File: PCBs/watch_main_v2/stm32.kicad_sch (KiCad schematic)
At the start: 20 parts, among them U801 STM32U5A9NJH6Q, Y801 16MHz, Y802 32.768kHz

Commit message: Schematic v2 complete
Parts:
- added R807, R808, R809, R810: 4k7, Resistor_SMD:R_0402_1005Metric, symbol Device:R_Small
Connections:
- net SWCLK is gone; now on net SWD.SWCLK: TP806.1
- net SWDIO is gone; now on net SWD.SWDIO: TP805.1
- net +1V8: now also R801.1, R802.1, R809.1, R810.1
- net +3V3: now also R807.1, R808.1; no longer R801.1, R802.1
- net ADF1_CCK0: now also U801.P9 (PE9)
- net ADF1_SDI0: now also U801.P10 (PE10)
- net CRS_SYNC: now also U801.D12 (PA10)
- net FLASH_CS2: now also U801.N4 (PA0)
- net I2C1.SCL: now also U801.D7 (PG14), R807.2; no longer R801.2
- net I2C1.SDA: now also U801.B6 (PG13), R808.2; no longer R802.2
- net I2C3.SCL: now also U801.P2 (PC0)
- net I2C3.SDA: now also U801.M1 (PC1)
- net I2C4.SCL: now also U801.M13 (PD12)
- net I2C4.SDA: now also U801.N14 (PD13)
- net LPUART1.RX: now also U801.E13 (PG8)
- net LPUART1.TX: now also U801.D13 (PG7)
- net LPUART1_CTS: now also U801.E14 (PG5)
- net LPUART1_RTS: now also U801.M6 (PB1)
- net OSPI1.CLKN: now also U801.M11 (PB12)
- net OSPI1.CLKP: now also U801.N12 (PB10)
- net OSPI1.CS: now also U801.P11 (PE11)
- net OSPI1.DQS: now also U801.D14 (PG6)
- net OSPI1.IO0: now also U801.J14 (PI3)
- net OSPI1.IO1: now also U801.J13 (PI2)
- net OSPI1.IO2: now also U801.J12 (PI1)
- net OSPI1.IO3: now also U801.D10 (PH8)
- net OSPI1.IO4: now also U801.M14 (PH9)
- net OSPI1.IO5: now also U801.L13 (PH10)
- net OSPI1.IO6: now also U801.L14 (PH11)
- net OSPI1.IO7: now also U801.M15 (PH12)
- net SDMMC1.CK: now also U801.C10 (PC12)
- net SDMMC1.CKIN: now also U801.C6 (PB8)
- net SDMMC1.CMD: now also U801.B9 (PD2)
- net SDMMC1.D0: now also U801.A14 (PC8)
- net SDMMC1.D1: now also U801.C14 (PC9)
- net SDMMC1.D2: now also U801.A10 (PC10)
- net SDMMC1.D3: now also U801.B10 (PC11)
- net SWO: now also U801.E7 (PB3)
- net USART6.RX: now also U801.P1 (PC2); no longer TP803.1
- net USART6.TX: now also U801.N3 (PC3); no longer TP802.1
- net SWD.SWCLK: now reaches U801.A12 (PA14)
- net USART1.RX: now reaches U801.A3 (PB7)
- net USART1.TX: now reaches U801.A4 (PB6)
- net USB.DP: now reaches U801.B13 (PA12)
- net USB.DN: now reaches U801.B14 (PA11)
- net SWD.SWDIO: now reaches U801.C13 (PA13)
- net GPIO2: now reaches U801.C9 (PD1)
- net GPIO1: now reaches U801.D9 (PD0)
- net I2C2.SCL: now reaches U801.M12 (PB13)
- net I2C2.SCL: now also R801.2
- net SPI1.CS: now reaches U801.N6 (PB0)
- net I2C2.SDA: now reaches U801.P13 (PB14)
- net I2C2.SDA: now also R802.2
- net SPI1.MISO: now reaches U801.P5 (PA6)
- net SPI1.SCK: now reaches U801.R4 (PA5)
- net SPI1.MOSI: now reaches U801.R5 (PA7)
- net I2C6.SCL: now reaches U801.F1 (PJ10)
- net I2C6.SCL: now also R809.2
- net I2C6.SDA: now reaches U801.H3 (PF0)
- net I2C6.SDA: now also R810.2
- net NRST renamed SWD.RST
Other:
- removed sheet STM32 Power
- moved on the sheet: C801, C802, C803, C804, R801, R802, R803, R804, R805, R806, TP804, TP805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

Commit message: 252 Unrouted traces
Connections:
- net GNSS_RST: now also U801.D1 (PJ3)
- net GNSS_WAKEUP: now also U801.E2 (PJ6)
- net TP_INT: now also U801.F2 (PJ8)
- net TP_RST: now also U801.E1 (PJ7)
- no-connect marks 4 -> 11
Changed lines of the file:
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@@
   (junction (at 243.84 236.22) (diameter 0) (color 0 0 0 0)
   )
+  (no_connect (at 195.58 157.48))
+  (no_connect (at 144.78 119.38))
   (no_connect (at 287.02 60.96))
+  (no_connect (at 144.78 109.22))
   (no_connect (at 287.02 63.5))
   (no_connect (at 287.02 81.28))
+  (no_connect (at 195.58 170.18))
+  (no_connect (at 195.58 60.96))
+  (no_connect (at 337.82 106.68))
   (no_connect (at 287.02 78.74))
+  (no_connect (at 195.58 167.64))
   (bus_entry (at 50.8 205.74) (size -2.54 2.54)
     (stroke (width 0) (type default))
@@
     (stroke (width 0) (type default))
   )
+  (wire (pts (xy 116.84 154.94) (xy 144.78 154.94))
+    (stroke (width 0) (type default))
+  )
   (wire (pts (xy 35.56 182.88) (xy 48.26 182.88))
     (stroke (width 0) (type default))
@@
     (stroke (width 0) (type default))
   )
-  (wire (pts (xy -15.24 83.82) (xy -43.18 83.82))
+  (wire (pts (xy 116.84 162.56) (xy 144.78 162.56))
     (stroke (width 0) (type default))
   )
@@
     (stroke (width 0) (type default))
   )
-  (wire (pts (xy -88.9 203.2) (xy -68.58 203.2))
-    (stroke (width 0) (type default))
-  )
   (wire (pts (xy 223.52 86.36) (xy 195.58 86.36))
     (stroke (width 0) (type default))
@@
     (stroke (width 0) (type default))
   )
+  (wire (pts (xy 116.84 165.1) (xy 144.78 165.1))
+    (stroke (width 0) (type default))
+  )
   (bus (pts (xy 50.8 50.8) (xy 71.12 50.8))
     (stroke (width 0) (type default))
@@
     (stroke (width 0) (type default))
   )
-  (wire (pts (xy -88.9 210.82) (xy -68.58 210.82))
-    (stroke (width 0) (type default))
-  )
   (wire (pts (xy 35.56 134.62) (xy 48.26 134.62))
     (stroke (width 0) (type default))
@@
     (stroke (width 0) (type default))
   )
+  (wire (pts (xy 116.84 167.64) (xy 144.78 167.64))
+    (stroke (width 0) (type default))
+  )
   (wire (pts (xy 337.82 160.02) (xy 363.22 160.02))
     (stroke (width 0) (type default))
@@
   )
   (wire (pts (xy 261.62 104.14) (xy 287.02 104.14))
-    (stroke (width 0) (type default))
-  )
-  (wire (pts (xy -99.06 96.52) (xy -71.12 96.52))
     (stroke (width 0) (type default))
   )
@@
     (effects (font (size 1.27 1.27)) (justify left bottom))
   )
+  (label "GNSS_RST" (at 119.38 154.94 0) (fields_autoplaced)
+    (effects (font (size 1.27 1.27)) (justify left bottom))
+  )
   (label "FLASH_INT" (at -15.24 195.58 180) (fields_autoplaced)
     (effects (font (size 1.27 1.27)) (justify right bottom))
@@
     (effects (font (size 1.27 1.27)) (justify right bottom))
   )
-  (label "GNSS_RST" (at -73.66 96.52 180) (fields_autoplaced)
-    (effects (font (size 1.27 1.27)) (justify right bottom))
-  )
   (label "DEBUG_LED" (at -15.24 157.48 180) (fields_autoplaced)
     (effects (font (size 1.27 1.27)) (justify right bottom))
@@
     (effects (font (size 1.27 1.27)) (justify left bottom))
   )
-  (label "GNSS_WAKEUP" (at -17.78 83.82 180) (fields_autoplaced)
-    (effects (font (size 1.27 1.27)) (justify right bottom))
+  (label "GNSS_WAKEUP" (at 119.38 162.56 0) (fields_autoplaced)
+    (effects (font (size 1.27 1.27)) (justify left bottom))
   )
   (label "I2C1.SDA" (at 35.56 144.78 0) (fields_autoplaced)
@@
     (effects (font (size 1.27 1.27)) (justify left bottom))
   )
-  (label "TP_INT" (at -86.36 210.82 0) (fields_autoplaced)
+  (label "TP_INT" (at 119.38 167.64 0) (fields_autoplaced)
     (effects (font (size 1.27 1.27)) (justify left bottom))
   )
@@
     (effects (font (size 1.27 1.27)) (justify left bottom))
   )
+  (label "TP_RST" (at 119.38 165.1 0) (fields_autoplaced)
+    (effects (font (size 1.27 1.27)) (justify left bottom))
+  )
   (label "IMU_INT1" (at -15.24 165.1 180) (fields_autoplaced)
     (effects (font (size 1.27 1.27)) (justify right bottom))
@@
   )
   (label "I2C2.SCL" (at 35.56 152.4 0) (fields_autoplaced)
-    (effects (font (size 1.27 1.27)) (justify left bottom))
-  )
-  (label "TP_RST" (at -86.36 203.2 0) (fields_autoplaced)
     (effects (font (size 1.27 1.27)) (justify left bottom))
   )
@@
     )
   )
-  (hierarchical_label "TP_INT" (shape input) (at -88.9 210.82 180) (fields_autoplaced)
+  (hierarchical_label "TP_INT" (shape input) (at 116.84 167.64 180) (fields_autoplaced)
     (effects (font (size 1.27 1.27)) (justify right))
   )
@@
     (effects (font (size 1.27 1.27)) (justify left))
   )
-  (hierarchical_label "GNSS_WAKEUP" (shape output) (at -15.24 83.82 0) (fields_autoplaced)
-    (effects (font (size 1.27 1.27)) (justify left))
+  (hierarchical_label "GNSS_WAKEUP" (shape output) (at 116.84 162.56 180) (fields_autoplaced)
+    (effects (font (size 1.27 1.27)) (justify right))
   )
   (hierarchical_label "CRS_SYNC" (shape input) (at 365.76 111.76 0) (fields_autoplaced)
     (effects (font (size 1.27 1.27)) (justify left))
-  )
-  (hierarchical_label "TP_RST" (shape output) (at -88.9 203.2 180) (fields_autoplaced)
-    (effects (font (size 1.27 1.27)) (justify right))
   )
   (hierarchical_label "BT_INT1" (shape bidirectional) (at -73.66 167.64 0) (fields_autoplaced)
@@
     )
   )
+  (hierarchical_label "TP_RST" (shape output) (at 116.84 165.1 180) (fields_autoplaced)
+    (effects (font (size 1.27 1.27)) (justify right))
+  )
   (hierarchical_label "GPIO2" (shape bidirectional) (at 259.08 132.08 180) (fields_autoplaced)
     (effects (font (size 1.27 1.27)) (justify right))
@@
     (effects (font (size 1.27 1.27)) (justify right))
   )
+  (hierarchical_label "GNSS_RST" (shape output) (at 116.84 154.94 180) (fields_autoplaced)
+    (effects (font (size 1.27 1.27)) (justify right))
+  )
   (hierarchical_label "FLASH_RSTO" (shape input) (at -12.7 193.04 0) (fields_autoplaced)
     (effects (font (size 1.27 1.27)) (justify left))
@@
     (effects (font (size 1.27 1.27)) (justify left))
   )
-  (hierarchical_label "GNSS_RST" (shape output) (at -71.12 96.52 0) (fields_autoplaced)
-    (effects (font (size 1.27 1.27)) (justify left))
-  )

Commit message: 262 Unrouted traces, fixed clearance issues
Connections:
- no-connect marks 11 -> 15
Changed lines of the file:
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@@
     (rev "2")
   )
+  (bus_alias "QSPI" (members "SCK" "IO0" "IO1" "IO2" "IO3" "CS"))
+  (bus_alias "I2C" (members "SCL" "SDA"))
+  (bus_alias "DSI-1" (members "CKN" "CKP" "D0N" "D0P"))
   (bus_alias "SDIO" (members "CK" "CKIN" "D0" "D1" "D2" "D3" "CMD"))
+  (bus_alias "USB" (members "DP" "DN"))
   (bus_alias "UART" (members "TX" "RX"))
-  (bus_alias "QSPI" (members "SCK" "IO0" "IO1" "IO2" "IO3" "CS"))
+  (bus_alias "SPI" (members "SCK" "MISO" "MOSI" "CS"))
   (bus_alias "DSI-2" (members "CKN" "CKP" "D0N" "D0P" "D1N" "D1P"))
-  (bus_alias "USB" (members "DP" "DN"))
-  (bus_alias "I2C" (members "SCL" "SDA"))
-  (bus_alias "SPI" (members "SCK" "MISO" "MOSI" "CS"))
-  (bus_alias "DSI-1" (members "CKN" "CKP" "D0N" "D0P"))
   (junction (at 144.78 251.46) (diameter 0) (color 0 0 0 0)
   )
@@
   (no_connect (at 287.02 60.96))
   (no_connect (at 144.78 109.22))
+  (no_connect (at 195.58 66.04))
+  (no_connect (at 195.58 162.56))
   (no_connect (at 287.02 63.5))
   (no_connect (at 287.02 81.28))
@@
   (no_connect (at 195.58 60.96))
   (no_connect (at 337.82 106.68))
+  (no_connect (at 337.82 162.56))
+  (no_connect (at 287.02 147.32))
   (no_connect (at 287.02 78.74))
   (no_connect (at 195.58 167.64))

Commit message: 190 Unrouted traces
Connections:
- net ALS_INT: now also U801.M2 (PF6)
- net BTN: now also U801.M8 (PE8)
- net HR_INT: now also U801.N15 (PD14)
- net IMU_INT1: now also U801.R7 (PB2)
- net IMU_INT2: now also U801.R8 (PF14)
- net LRA_EN: now also U801.P15 (PD9)
- net MAG_INT: now also U801.R6 (PC4)
- net PWR_ENCHG: now also U801.R14 (PB15)
- net PWR_INT: now also U801.P14 (PD10)
- net TOUCH_INT: now also U801.N9 (PE7)
- net TOUCH_RST: now also U801.N11 (PE12)
- no-connect marks 15 -> 28

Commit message: Main board v2 complete
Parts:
- removed TP801, TP802, TP803: 1.5mm, TestPoint:TestPoint_Pad_D1.5mm, symbol Connector:TestPoint_Small
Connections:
- net AVDDEN: now also U801.A7 (PG9)
- net BT_INT1: now also U801.B15 (PC7)
- net BT_INT2: now also U801.C15 (PC6)
- net DISPLAY_RST: now also U801.L3 (PF7)
- net FLASH_INT: now also U801.F15 (PI13)
- net FLASH_RST: now also U801.F14 (PI14)
- net FLASH_RSTO: now also U801.G15 (PI10)
- net SD_CD: now also U801.A9 (PD3)
- net SWIRE: now also U801.A6 (PG12), U801.B7 (PG10)
- net SD_EN: now reaches U801.A8 (PD4)
- no-connect marks 28 -> 76

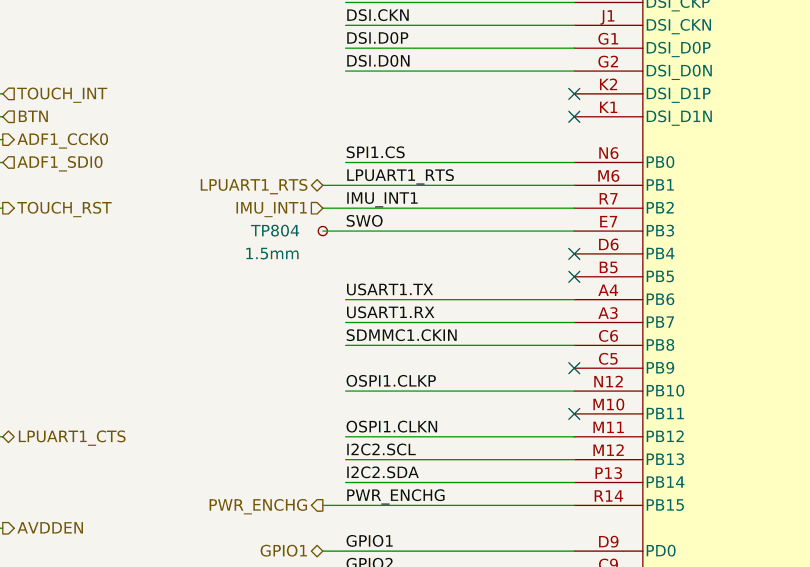
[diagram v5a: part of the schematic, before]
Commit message: Added EEPROM
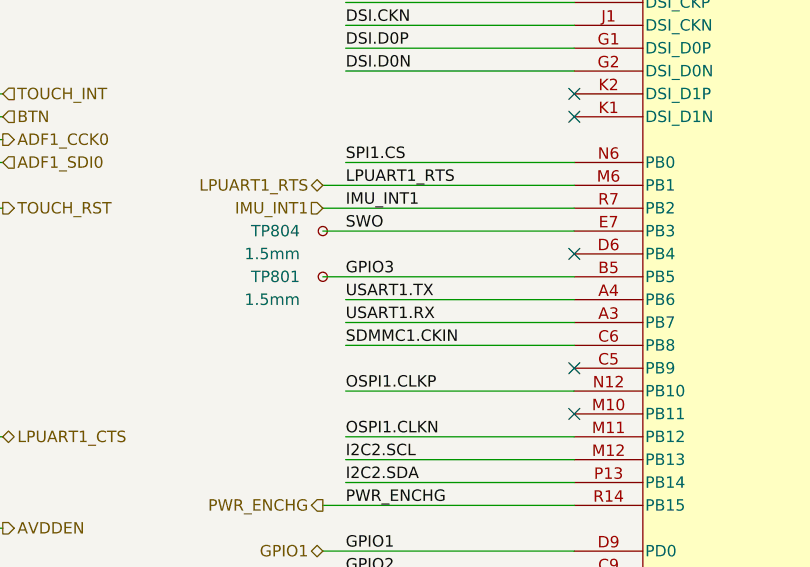
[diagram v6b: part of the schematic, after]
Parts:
- added TP801: 1.5mm, TestPoint:TestPoint_Pad_D1.5mm, symbol Connector:TestPoint_Small
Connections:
- net GPIO3: now reaches U801.B5 (PB5)
- net GPIO3: now also TP801.1
- no-connect marks 76 -> 75
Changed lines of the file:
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@@
     (rev "2")
   )
-  (bus_alias "DSI-1" (members "CKN" "CKP" "D0N" "D0P"))
-  (bus_alias "UART" (members "TX" "RX"))
+  (bus_alias "USB" (members "DP" "DN"))
+  (bus_alias "I2C" (members "SCL" "SDA"))
   (bus_alias "SPI" (members "SCK" "MISO" "MOSI" "CS"))
-  (bus_alias "DSI-2" (members "CKN" "CKP" "D0N" "D0P" "D1N" "D1P"))
   (bus_alias "QSPI" (members "SCK" "IO0" "IO1" "IO2" "IO3" "CS"))
-  (bus_alias "I2C" (members "SCL" "SDA"))
+  (bus_alias "UART" (members "TX" "RX"))
+  (bus_alias "DSI-2" (members "CKN" "CKP" "D0N" "D0P" "D1N" "D1P"))
   (bus_alias "SDIO" (members "CK" "CKIN" "D0" "D1" "D2" "D3" "CMD"))
-  (bus_alias "USB" (members "DP" "DN"))
+  (bus_alias "DSI-1" (members "CKN" "CKP" "D0N" "D0P"))
   (junction (at 144.78 251.46) (diameter 0) (color 0 0 0 0)
   )
@@
   (no_connect (at 195.58 66.04))
   (no_connect (at 195.58 142.24))
-  (no_connect (at 287.02 99.06))
   (no_connect (at 144.78 68.58))
   (no_connect (at 195.58 162.56))
@@
     (stroke (width 0) (type default))
   )
+  (wire (pts (xy 259.08 99.06) (xy 287.02 99.06))
+    (stroke (width 0) (type default))
+  )
   (wire (pts (xy 195.58 127) (xy 223.52 127))
     (stroke (width 0) (type default))
@@
     (effects (font (size 1.27 1.27)) (justify left bottom))
   )
+  (label "GPIO3" (at 261.62 99.06 0) (fields_autoplaced)
+    (effects (font (size 1.27 1.27)) (justify left bottom))
+  )
   (label "ALS_INT" (at 119.38 76.2 0) (fields_autoplaced)
     (effects (font (size 1.27 1.27)) (justify left bottom))
@@
         )
       )
+    )
+  )
+  (symbol (lib_id "Connector:TestPoint_Small") (at 259.08 99.06 0) (mirror y) (unit 1)
+    (in_bom yes) (on_board yes) (dnp no)
+    (property "Reference" "TP801" (at 256.54 99.06 0)
+      (effects (font (size 1.27 1.27)) (justify left))
+    )
+    (property "Value" "1.5mm" (at 256.54 101.6 0)
+      (effects (font (size 1.27 1.27)) (justify left))
+    )
+    (property "Footprint" "TestPoint:TestPoint_Pad_D1.5mm" (at 254 99.06 0)
+      (effects (font (size 1.27 1.27)) hide)
+    )
+    (property "Datasheet" "~" (at 254 99.06 0)
+      (effects (font (size 1.27 1.27)) hide)
+    )
+    (pin "1")
+    (instances
+      (project "watch_main"
+        (path "/b008648a-c7cf-4e14-8a0a-b9314d757b4a/8f147234-e39a-4c7c-8011-0af923cea553"
+          (reference "TP801") (unit 1)
+        )
+      )

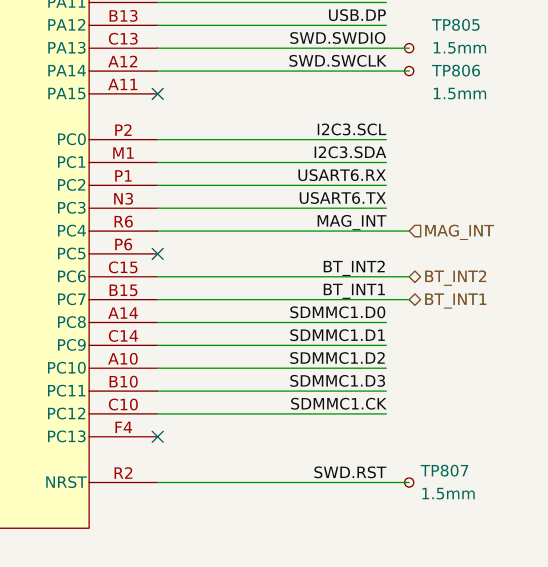
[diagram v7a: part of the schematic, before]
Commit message: Default firmware finished, minor main PCB update
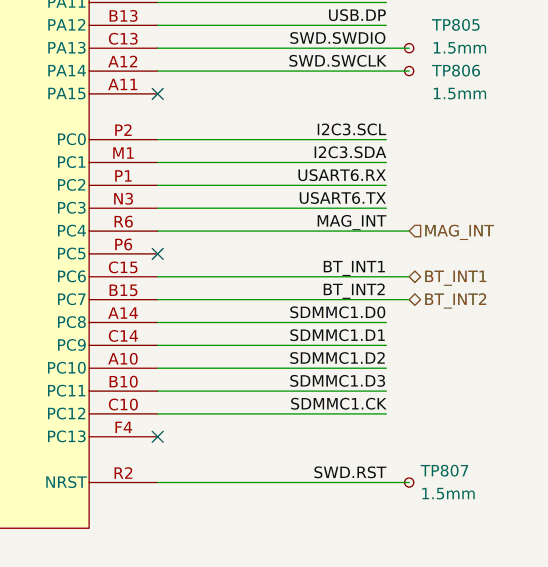
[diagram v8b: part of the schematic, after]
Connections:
- net BT_INT1: now also U801.C15 (PC6); no longer U801.B15 (PC7)
- net BT_INT2: now also U801.B15 (PC7); no longer U801.C15 (PC6)
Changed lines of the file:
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@@
     (rev "2")
   )
+  (bus_alias "DSI-1" (members "CKN" "CKP" "D0N" "D0P"))
+  (bus_alias "DSI-2" (members "CKN" "CKP" "D0N" "D0P" "D1N" "D1P"))
   (bus_alias "I2C" (members "SCL" "SDA"))
+  (bus_alias "QSPI" (members "SCK" "IO0" "IO1" "IO2" "IO3" "CS"))
+  (bus_alias "SDIO" (members "CK" "CKIN" "D0" "D1" "D2" "D3" "CMD"))
   (bus_alias "SPI" (members "SCK" "MISO" "MOSI" "CS"))
-  (bus_alias "DSI-2" (members "CKN" "CKP" "D0N" "D0P" "D1N" "D1P"))
-  (bus_alias "SDIO" (members "CK" "CKIN" "D0" "D1" "D2" "D3" "CMD"))
-  (bus_alias "QSPI" (members "SCK" "IO0" "IO1" "IO2" "IO3" "CS"))
+  (bus_alias "UART" (members "TX" "RX"))
   (bus_alias "USB" (members "DP" "DN"))
-  (bus_alias "UART" (members "TX" "RX"))
-  (bus_alias "DSI-1" (members "CKN" "CKP" "D0N" "D0P"))
   (junction (at 144.78 251.46) (diameter 0) (color 0 0 0 0)
   )
@@
     (effects (font (size 1.27 1.27)) (justify left bottom))
   )
-  (label "BT_INT1" (at 363.22 147.32 180) (fields_autoplaced)
+  (label "BT_INT1" (at 363.22 144.78 180) (fields_autoplaced)
     (effects (font (size 1.27 1.27)) (justify right bottom))
   )
@@
     (effects (font (size 1.27 1.27)) (justify left bottom))
   )
-  (label "BT_INT2" (at 363.22 144.78 180) (fields_autoplaced)
+  (label "BT_INT2" (at 363.22 147.32 180) (fields_autoplaced)
     (effects (font (size 1.27 1.27)) (justify right bottom))
   )
@@
     (effects (font (size 1.27 1.27)) (justify right))
   )
-  (hierarchical_label "BT_INT2" (shape bidirectional) (at 365.76 144.78 0) (fields_autoplaced)
+  (hierarchical_label "BT_INT2" (shape bidirectional) (at 365.76 147.32 0) (fields_autoplaced)
     (effects (font (size 1.27 1.27)) (justify left))
   )
@@
     (effects (font (size 1.27 1.27)) (justify left))
   )
-  (hierarchical_label "BT_INT1" (shape bidirectional) (at 365.76 147.32 0) (fields_autoplaced)
+  (hierarchical_label "BT_INT1" (shape bidirectional) (at 365.76 144.78 0) (fields_autoplaced)
     (effects (font (size 1.27 1.27)) (justify left))
   )
